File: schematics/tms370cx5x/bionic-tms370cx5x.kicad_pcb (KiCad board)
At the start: 2 copper layers, 31.7 x 68.6 mm, 11 parts, among them J1 Bionic-P135, J2 Bionic-P245, U1 TMS370C250, U2 11AA010-I/TT

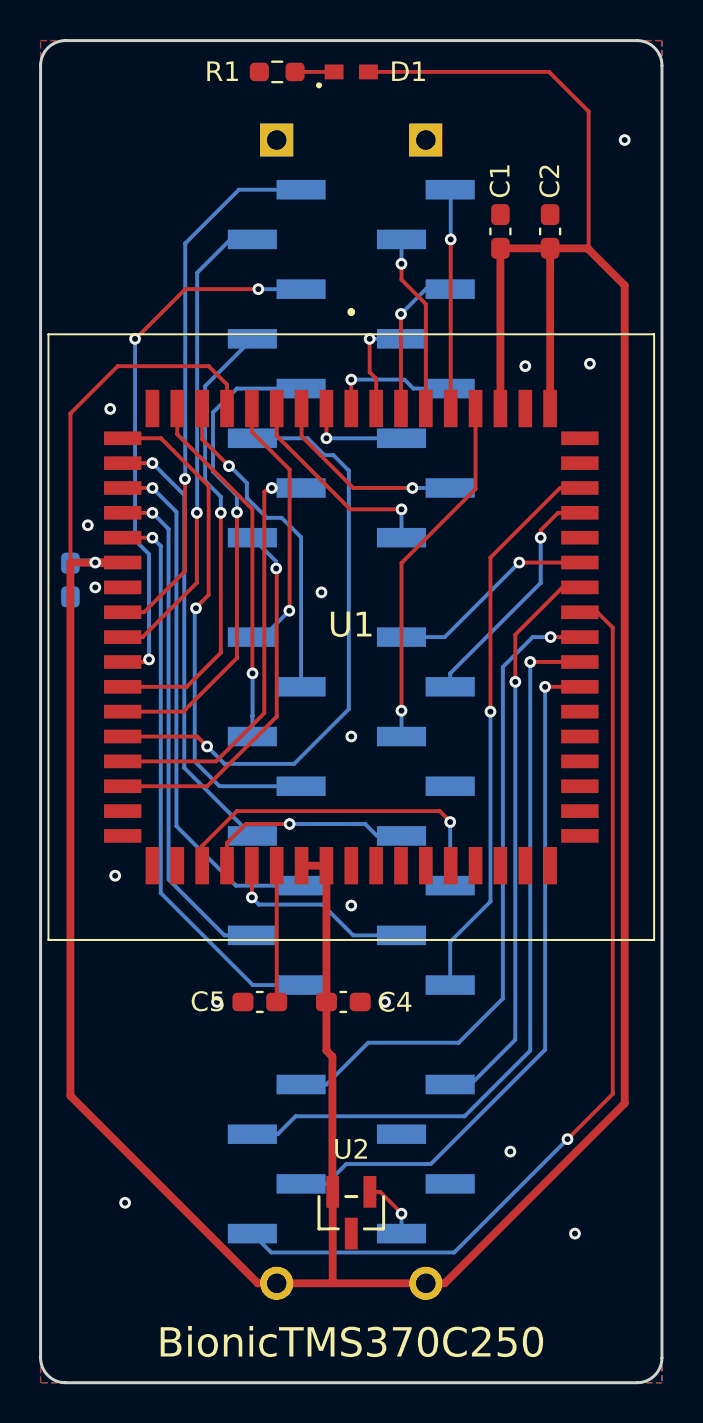
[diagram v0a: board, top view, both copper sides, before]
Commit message: [TMS370Cx5x] Rename TMS370C250 to TNS370Cx5x
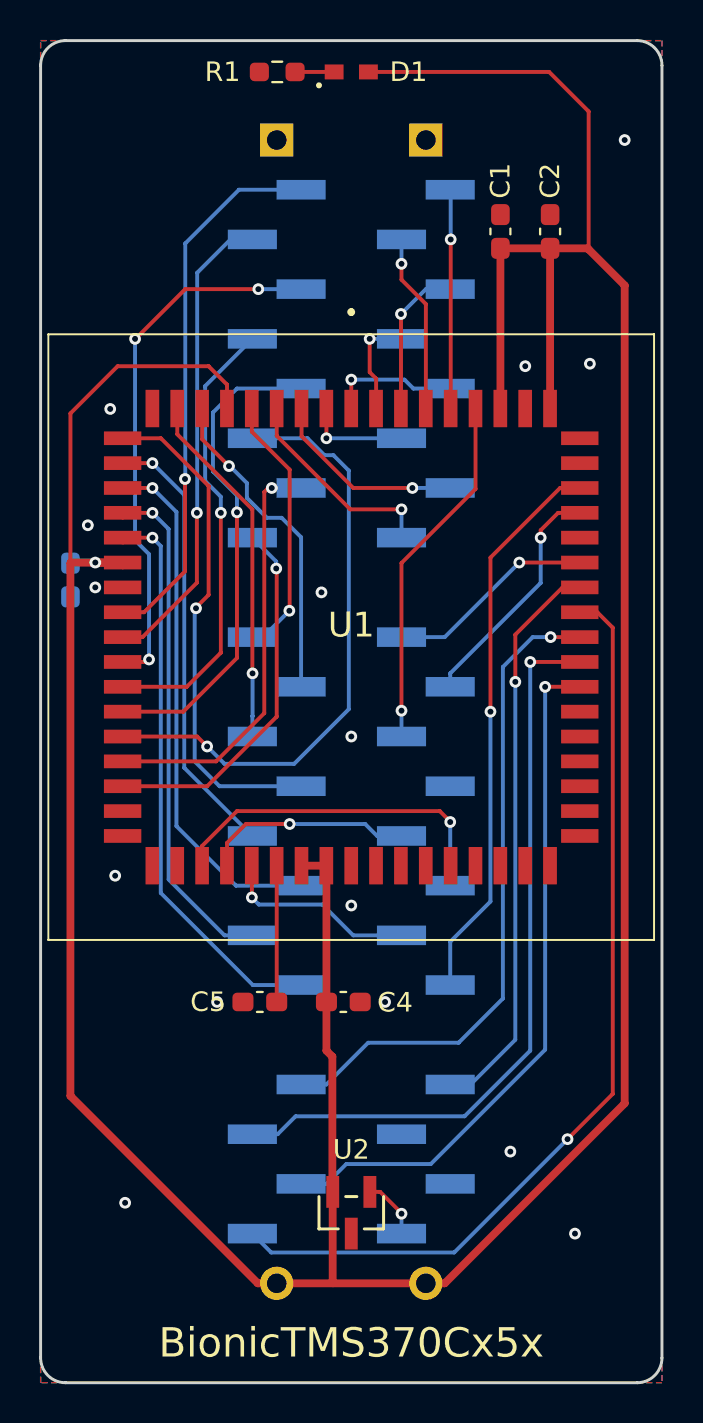
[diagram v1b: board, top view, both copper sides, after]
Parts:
- U1: value TMS370C250 -> TMS370Cx5x
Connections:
- U1 pad 35: GND -> unconnected-(U1-VSS_{3}-Pad35)
- U1 pad 9: GND -> unconnected-(U1-VSS_{1}-Pad9)
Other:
- board text added: "BionicTMS370Cx5x"
- board text removed: "BionicTMS370C250"
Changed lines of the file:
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@@
 	(paper "A4")
 	(title_block
-		(title "BionicTMS370C250")
+		(title "BionicTMS370Cx5x")
 		(date "2026-02-01")
 		(rev "3")
@@
 	(net 64 "unconnected-(U1-SPISOMI-Pad49)")
 	(net 65 "unconnected-(U1-AN5-Pad41)")
+	(net 66 "unconnected-(U1-VSS_{3}-Pad35)")
+	(net 67 "unconnected-(U1-VSS_{1}-Pad9)")
 	(footprint "rhom:LED_CSL1901UW1_ROM-M"
 		(layer "F.Cu")
@@
 		(property ki_fp_filters "LED_CSL1901UW1_ROM LED_CSL1901UW1_ROM-M LED_CSL1901UW1_ROM-L")
 		(sheetname "/")
-		(sheetfile "bionic-tms370c250.kicad_sch")
+		(sheetfile "bionic-tms370cx5x.kicad_sch")
 		(attr smd)
 		(fp_circle
@@
 	(footprint "3m:846821B1RKTP"
 		(layer "F.Cu")
-		(at 113.7 100.48)
+		(at 113.696 100.48)
 		(descr "8468-21B1-RK-TP-2")
 		(tags "Connector")
@@
 			)
 		)
-		(property "Value" "TMS370C250"
+		(property "Value" "TMS370Cx5x"
 			(at 0 -0.618 0)
 			(layer "F.SilkS")
@@
 		(property ki_fp_filters "PLCC-68*")
 		(sheetname "/")
-		(sheetfile "bionic-tms370c250.kicad_sch")
+		(sheetfile "bionic-tms370cx5x.kicad_sch")
 		(attr smd)
 		(fp_line
@@
 			(size 0.7 1.91)
 			(layers "F.Cu" "F.Mask" "F.Paste")
-			(net 2 "GND")
+			(net 67 "unconnected-(U1-VSS_{1}-Pad9)")
 			(pinfunction "VSS_{1}")
 			(pintype "power_in")
@@
 			(size 0.7 1.91)
 			(layers "F.Cu" "F.Mask" "F.Paste")
-			(net 2 "GND")
+			(net 66 "unconnected-(U1-VSS_{3}-Pad35)")
 			(pinfunction "VSS_{3}")
 			(pintype "power_in")
@@
 		(property ki_fp_filters "C_*")
 		(sheetname "/")
-		(sheetfile "bionic-tms370c250.kicad_sch")
+		(sheetfile "bionic-tms370cx5x.kicad_sch")
 		(attr smd)
 		(fp_line
@@
 		(property ki_fp_filters "C_*")
 		(sheetname "/")
-		(sheetfile "bionic-tms370c250.kicad_sch")
+		(sheetfile "bionic-tms370cx5x.kicad_sch")
 		(attr smd)
 		(fp_line
@@
 		(property ki_fp_filters "C_*")
 		(sheetname "/")
-		(sheetfile "bionic-tms370c250.kicad_sch")
+		(sheetfile "bionic-tms370cx5x.kicad_sch")
 		(attr smd)
 		(fp_line
@@
 		(property ki_fp_filters "R_*")
 		(sheetname "/")
-		(sheetfile "bionic-tms370c250.kicad_sch")
+		(sheetfile "bionic-tms370cx5x.kicad_sch")
 		(attr smd)
 		(fp_line
@@
 		(property ki_fp_filters "SOT-23_MC_MCH")
 		(sheetname "/")
-		(sheetfile "bionic-tms370c250.kicad_sch")
+		(sheetfile "bionic-tms370cx5x.kicad_sch")
 		(attr smd)
 		(fp_line
@@
 		(property ki_fp_filters "C_*")
 		(sheetname "/")
-		(sheetfile "bionic-tms370c250.kicad_sch")
+		(sheetfile "bionic-tms370cx5x.kicad_sch")
 		(attr smd)
 		(fp_line
@@
 		(property ki_fp_filters "Bionic-P245*")
 		(sheetname "/")
-		(sheetfile "bionic-tms370c250.kicad_sch")
+		(sheetfile "bionic-tms370cx5x.kicad_sch")
 		(attr through_hole allow_soldermask_bridges)
 		(fp_line
@@
 		(property ki_fp_filters "C_*")
 		(sheetname "/")
-		(sheetfile "bionic-tms370c250.kicad_sch")
+		(sheetfile "bionic-tms370cx5x.kicad_sch")
 		(attr smd)
 		(fp_line
@@
 		(property ki_fp_filters "Bionic-P135*")
 		(sheetname "/")
-		(sheetfile "bionic-tms370c250.kicad_sch")
+		(sheetfile "bionic-tms370cx5x.kicad_sch")
 		(attr through_hole)
 		(fp_line
@@
 		(layer "Edge.Cuts")
 	)
-	(gr_text "BionicTMS370C250"
+	(gr_text "BionicTMS370Cx5x"
 		(at 113.7 136.548 0)
 		(layer "F.SilkS")
@@
 			)
 		)
-		(render_cache "BionicTMS370C250" 0
+		(render_cache "BionicTMS370Cx5x" 0
 			(polygon
 				(pts
@@
 			(polygon
 				(pts
-					(xy 121.089475 137.1705) (xy 120.156071 137.1705) (xy 120.156071 137.010673) (xy 120.51465 136.620678)
-					(xy 120.694064 136.413426) (xy 120.777974 136.295713) (xy 120.813195 136.222201) (xy 120.834356 136.143992)
-					(xy 120.841538 136.059775) (xy 120.83368 135.985625) (xy 120.811698 135.926066) (xy 120.776417 135.877875)
-					(xy 120.72926 135.841487) (xy 120.671706 135.819063) (xy 120.600745 135.811105) (xy 120.522419 135.819077)
-					(xy 120.442899 135.843581) (xy 120.360778 135.886397) (xy 120.274864 135.950415) (xy 120.170359 135.828507)
-					(xy 120.274274 135.749429) (xy 120.379987 135.695064) (xy 120.488877 135.663006) (xy 120.60276 135.652286)
-					(xy 120.701698 135.659819) (xy 120.785263 135.68107) (xy 120.856132 135.714789) (xy 120.916368 135.760821)
-					(xy 120.965781 135.81855) (xy 121.001314 135.885143) (xy 121.023382 135.962338) (xy 121.031132 136.052539)
-					(xy 121.024721 136.132531) (xy 121.004976 136.215451) (xy 120.970682 136.302308) (xy 120.922281 136.384954)
-					(xy 120.828994 136.50841) (xy 120.672461 136.686166) (xy 120.384499 136.992263) (xy 120.384499 137.000415)
-					(xy 121.089475 137.000415)
+					(xy 120.516756 136.593384) (xy 120.11403 136.045028) (xy 120.326155 136.045028) (xy 120.623277 136.465248)
+					(xy 120.921497 136.045028) (xy 121.133622 136.045028) (xy 120.72879 136.593384) (xy 121.152032 137.1705)
+					(xy 120.940915 137.1705) (xy 120.623277 136.723627) (xy 120.304631 137.1705) (xy 120.092507 137.1705)
 				)
 			)
@@
 			(polygon
 				(pts
-					(xy 123.231599 135.654805) (xy 123.311842 135.678827) (xy 123.38203 135.717859) (xy 123.44383 135.772688)
-					(xy 123.498046 135.845452) (xy 123.547057 135.945187) (xy 123.585178 136.070514) (xy 123.61032 136.226671)
-					(xy 123.619495 136.419636) (xy 123.610817 136.613762) (xy 123.587126 136.769394) (xy 123.551423 136.892798)
-					(xy 123.505909 136.989505) (xy 123.451856 137.064177) (xy 123.38948 137.120409) (xy 123.317918 137.160501)
-					(xy 123.235295 137.185267) (xy 123.138917 137.193947) (xy 123.04761 137.18561) (xy 122.968362 137.161681)
-					(xy 122.898842 137.122731) (xy 122.83743 137.067906) (xy 122.783361 136.995011) (xy 122.73461 136.895281)
-					(xy 122.696657 136.769791) (xy 122.671607 136.613252) (xy 122.66246 136.419636) (xy 122.66248 136.419178)
-					(xy 122.851962 136.419178) (xy 122.857628 136.591671) (xy 122.872682 136.722834) (xy 122.894535 136.820328)
-					(xy 122.921113 136.890964) (xy 122.962274 136.955978) (xy 123.011259 136.999822) (xy 123.069183 137.026012)
-					(xy 123.138917 137.035128) (xy 123.209653 137.025961) (xy 123.268478 136.99963) (xy 123.318277 136.955597)
-					(xy 123.360201 136.890414) (xy 123.38743 136.819475) (xy 123.409768 136.721905) (xy 123.425132 136.590991)
-					(xy 123.430909 136.419178) (xy 123.425144 136.248511) (xy 123.409798 136.118229) (xy 123.387463 136.02091)
-					(xy 123.360201 135.949957) (xy 123.318277 135.884774) (xy 123.268478 135.840741) (xy 123.209653 135.81441)
-					(xy 123.138917 135.805243) (xy 123.069151 135.814339) (xy 123.011218 135.840463) (xy 122.962247 135.884173)
-					(xy 122.921113 135.948949) (xy 122.894535 136.019327) (xy 122.872683 136.116484) (xy 122.857629 136.247217)
-					(xy 122.851962 136.419178) (xy 122.66248 136.419178) (xy 122.671091 136.225507) (xy 122.694645 136.069943)
-					(xy 122.730129 135.946664) (xy 122.775336 135.850124) (xy 122.828986 135.775646) (xy 122.890842 135.719612)
-					(xy 122.961748 135.679696) (xy 123.04355 135.655057) (xy 123.138917 135.646424)
+					(xy 123.034412 136.593384) (xy 122.631686 136.045028) (xy 122.843811 136.045028) (xy 123.140932 136.465248)
+					(xy 123.439153 136.045028) (xy 123.651277 136.045028) (xy 123.246445 136.593384) (xy 123.669687 137.1705)
+					(xy 123.45857 137.1705) (xy 123.140932 136.723627) (xy 122.822287 137.1705) (xy 122.610162 137.1705)
 				)
 			)
